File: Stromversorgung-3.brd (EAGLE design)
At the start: 35.2 x 53.3 mm, 17 parts, among them IC1 MCP2515-I/SO, IC2 MCP2562-E/SN, Q1 16MHz, X1 RASPI_GPIO_B+#_PIN

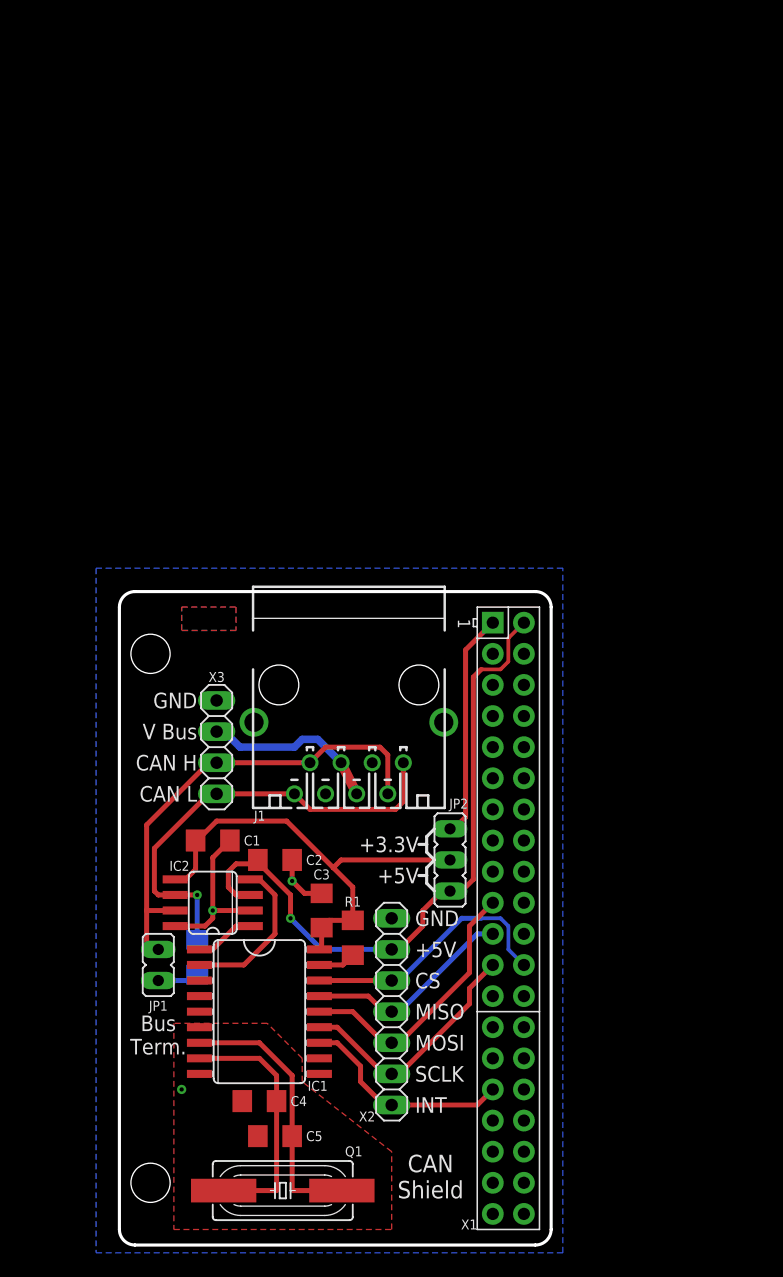
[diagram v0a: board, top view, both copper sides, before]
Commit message: Verbesserte Stromversorgung, Pi-Kühler, CAN-Bus 8x-Schalter
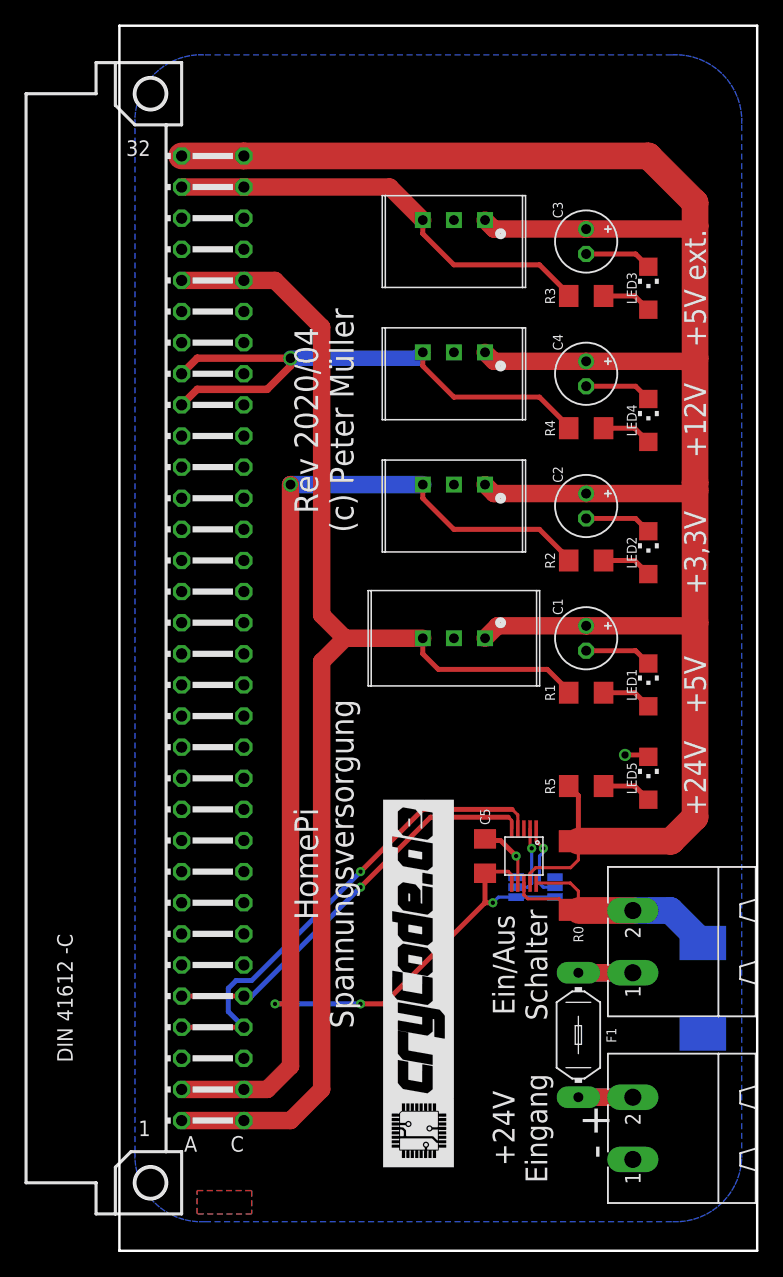
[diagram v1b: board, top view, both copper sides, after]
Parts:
- removed IC2: MCP2562-E/SN, mcp2515_2551_2562:SO08
- removed J1: (no value), can-bus:MEBP_8-8G
- removed JP1: (no value), jumper:JP1
- removed JP2: (no value), jumper:JP2
- removed Q1: 16MHz, crystal:HC49UP
- added A0, A1: JUMPER-SMT_3_NO_NO-SILK, SparkFun-Jumpers:SMT-JUMPER_3_NO_NO-SILK
- added D1: MBRS 540T3G, diode:SMC
- added F1: 30V / 2,5A, fuse:LITTLEFUSE
- added LED1, LED2, LED3, LED4, LED5: 2mA bl, led:CHIPLED_1206
- added R0: 0,02 1% 5W, rcl:R2512
- added R3: 1k2, rcl:R1206
- added R4: 4k7, rcl:R1206
- added R5: 12k, rcl:R1206
- added U1: TSR2-2450, TSR:TSR2
- added U2: TSR1-2433, TSR:TSR1
- added U3: TSR1-2450, TSR:TSR1
- added U4: TSR1-24120, TSR:TSR1
- C1, C2, C3: value 100nF -> 22µF 50V Low-ESR; device rcl:C1206 -> rcl:E2-5
- C4: value 22pF -> 22µF 50V Low-ESR; device rcl:C1206 -> rcl:E2-5
- C5: value 22pF -> (none)
- IC1: value MCP2515-I/SO -> TI-INA226; device mcp2515_2551_2562:SO18L -> FaBo-Sensor:TI-INA226
- R1: value 4k7 -> 1k2
- R2: value 120R -> 330
- X1: value RASPI_GPIO_B+#_PIN -> Ein/Aus; device raspberrypi_bastelstube_v13:RASPI_GPIO_B+_PIN -> con-phoenix-508:MSTBA2
- X2: value (none) -> MAC64L; device pinhead:1X07 -> con-vg:MAC64L
- X3: value (none) -> Eingang; device pinhead:1X04 -> con-phoenix-508:MSTBA2
- moved C4 65.1 mm to (38.1, 71.1), turned to 270 degrees
- moved C3 58.7 mm to (38.1, 81.9), turned to 270 degrees
- moved X3 49.9 mm to (47.0, 9.53), turned to 90 degrees
- moved R2 45.4 mm to (38.1, 55.9), flipped to the top, turned to 180 degrees
- moved C2 38.5 mm to (38.1, 60.3), turned to 270 degrees
- moved X2 36.3 mm to (2.54, 49.5), turned to 180 degrees
- moved C1 34.7 mm to (38.1, 49.5), turned to 270 degrees
- moved C5 28.6 mm to (29.8, 31.8), turned to 90 degrees
- moved R1 27.6 mm to (38.1, 45.1), turned to 180 degrees
- moved U$1 26.3 mm to (27.3, 6.35), flipped to the top, turned to 90 degrees
- moved IC1 25.0 mm to (33.0, 31.8)
- moved X1 15.4 mm to (47.0, 24.8), turned to 90 degrees
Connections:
- removed net +5V: C2.1, IC2.3, JP2.3, X1.2, X2.2
- removed net 3V3B: X1.17
- removed net 5V0B: X1.4
- removed net CANH: IC2.7, J1.2, J1.7, JP1.1, X3.3
- removed net CANL: IC2.6, J1.1, J1.8, R2.1, X3.4
- removed net GND_B: X1.9
- removed net GND_C: X1.14
- removed net GND_D: X1.20
- removed net GND_E: X1.25
- removed net GND_F: X1.30
- removed net GND_G: X1.34
- removed net GND_H: X1.39
- removed net GPIO.06: IC1.12, X1.31, X2.7
- removed net MCP_VCC: C1.1, C3.1, IC1.18, IC2.5, JP2.2, R1.2
- removed net N$4: C5.1, IC1.7, Q1.1
- removed net RXCAN: IC1.2, IC2.4
- removed net SPI_CE0: IC1.16, X1.24, X2.3
- removed net SPI_MISO: IC1.15, X1.21, X2.4
- removed net SPI_MOSI: IC1.14, X1.19, X2.5
- removed net SPI_SCLK: IC1.13, X1.23, X2.6
- removed net TXCAN: IC1.1, IC2.1
- new net !PI_RESET: X2.C7
- new net +12V: R4.2, U4.3, X2.A24, X2.A25
- new net +24V_1: D1.C, IC1.10, IC1.8, R0.2, X1.2
- new net +24V_IN: F1.1, X1.1
- new net +24V_IN_RAW: F1.2, X3.2
- new net +5V_EXT: R3.2, U3.3, X2.A31, X2.C31
- new net +5V_INT: R1.2, U1.3, X2.A1, X2.A28, X2.C1, X2.C28
- new net 1WIRE: X2.A7
- new net I2C_SCL: IC1.5, X2.A5, X2.C5
- new net I2C_SDA: IC1.4, X2.A4, X2.C4
- new net N$6: LED1.A, R1.1
- new net N$7: LED2.A, R2.1
- new net N$8: LED3.A, R3.1
- new net N$9: LED4.A, R4.1
- net +24V: now also C1.+, C2.+, C3.+, C4.+, IC1.9, R0.1, R5.2, U1.1, U2.1, U3.1, U4.1, X2.A32, X2.C32; no longer J1.4, J1.5, X3.2
- net +3,3V: now also A0.3, A1.3, C5.1, IC1.6, R2.2, U2.3, X2.A2, X2.C2; no longer JP2.1, X1.1
- net GND: now also A0.1, A1.1, C1.-, C2.-, C3.-, C4.-, D1.A, IC1.7, LED1.C, LED2.C, LED3.C, LED4.C, LED5.C, U1.2, U2.2, U3.2, U4.2, X2.A11, X2.A13, X2.A27, X2.A29, X2.A3, X2.A30, X2.A6, X2.A8, X2.C13, X2.C29, X2.C3, X2.C30, X2.C6, X2.C8; no longer C1.2, C2.2, C3.2, C4.2, IC1.9, IC2.2, IC2.8, J1.3, J1.6, J1.G1, J1.G2, X1.6, X2.1
- net N$1: now also A0.2, IC1.2; no longer C4.1, IC1.8, Q1.2
- net N$2: now also A1.2, IC1.1; no longer IC1.17, R1.1
- net N$3: now also LED5.A, R5.1; no longer JP1.2, R2.2
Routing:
- net +24V: track 14.6 -> 186.1 mm
- net +5V_INT: track 0.00 -> 110.2 mm
- net +3,3V: track 18.5 -> 116.4 mm, vias 0 -> 4
- net +5V: track 54.6 -> 0.00 mm, vias 1 -> 0
- net +12V: track 0.00 -> 46.5 mm, vias 0 -> 1
- net I2C_SDA: track 0.00 -> 39.8 mm, vias 0 -> 1
- net CANH: track 39.0 -> 0.00 mm
- net MCP_VCC: track 37.2 -> 0.00 mm
- net CANL: track 36.9 -> 0.00 mm, vias 1 -> 0
- net +5V_EXT: track 0.00 -> 36.0 mm
- net I2C_SCL: track 0.00 -> 33.8 mm, vias 0 -> 1
- net +24V_1: track 0.00 -> 22.5 mm
- net SPI_MOSI: track 22.2 -> 0.00 mm
- net N$4: track 22.1 -> 0.00 mm
- net SPI_CE0: track 21.5 -> 0.00 mm
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- removed copper zone on layer 16, net BOT
- removed copper zone on layer 1, net GND
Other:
- board size 35.2 x 53.3 mm -> 52.1 x 100 mm
- board text added: "+"
- board text added: "+12V"
- board text added: "+24V"
- board text added: "+24V Eingang"
- board text added: "+3,3V"
- board text added: "+5V ext."
- board text added: "-"
- board text added: "Ein/Aus Schalter"
- board text added: "HomePi Spannungsversorgung"
- board text added: "Rev 2020/04 (c) Peter Müller"
- board text removed: "+3.3V"
- board text removed: "Bus Term."
- board text removed: "CAN H"
- board text removed: "CAN L"
- board text removed: "CAN Shield"
- board text removed: "CS"
- board text removed: "GND"
- board text removed: "HomePi CAN-Bus"
- board text removed: "INT"
- board text removed: "MISO"
- board text removed: "MOSI"
- board text removed: "Raspbarry Pi / Universal CAN-Shield Rev. 2020/04 (C) 2020 Peter Müller <peter@crycode.de>"
- board text removed: "SCLK"
- board text removed: "V Bus"
- board text removed: "V+"

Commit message: Werte von Bauteilen angepasst
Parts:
- C5: value (none) -> 100nF
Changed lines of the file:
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@@
 <attribute name="VALUE" x="34.29" y="32.7025" size="1.27" layer="27" rot="R270"/>
 </element>
-<element name="C5" library="rcl" package="C1206" value="" x="29.845" y="31.75" smashed="yes" rot="R90">
+<element name="C5" library="rcl" package="C1206" value="100nF" x="29.845" y="31.75" smashed="yes" rot="R90">
 <attribute name="NAME" x="29.845" y="34.29" size="0.8128" layer="25" font="vector" rot="R90" align="center-left"/>
 <attribute name="VALUE" x="32.385" y="30.48" size="1.27" layer="27" rot="R90"/>
